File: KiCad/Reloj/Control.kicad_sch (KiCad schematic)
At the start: 67 parts, among them J13 Conn_01x08_SocketMPU, J14 Conn_01x04_Socket, J15 Screw_Terminal_01x02, J16 Conn_01x02, J17 Conn_01x06_Socket, J18 Conn_01x02, J19 Conn_01x03, J20 Conn_01x02, J21 Conn_01x02, Q1 BC548, Q2 BC548, Q3 BC548, Q4 BC548, Q5 BC548, Q6 BC548, Q7 BC548, SW1 SW_SPDT, SW2 SW_Push, SW3 SW_Push, SW4 SW_Push, SW5 SW_Push, U1 74HC14, U3 74HCT595

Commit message: Actualizo circuito y defino alimentaciones
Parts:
- added J1: Jack-DC, symbol Connector:Jack-DC
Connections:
- net 5v: now also U3.16 (VCC), J1.2
- net GND: now also J1.1
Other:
- note added: "ALIMENTACION EXTERNA Fte. 5Vdc"

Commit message: Agrego nueva numeracion de componentes e impresion de pdf
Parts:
- added C6: 0.1uF, symbol Device:C
- C5: value C -> 0.1uF
- R23: renamed from R18; value R_Small_US -> 330
- renumbered C6 to C1, C7 to C2, C8 to C3, C9 to C4, D4 to D1, D5 to D2, D2 to D3, D3 to D4, R4 to R1, R22 to R10, R23 to R11, R24 to R12, R25 to R13, R26 to R14, R19 to R15, R20 to R16, R12 to R17, R13 to R18, R14 to R19, R5 to R2, R15 to R20, R16 to R21, R17 to R22, R6 to R3, R7 to R4, R8 to R5, R9 to R6, R10 to R7, R11 to R8, R21 to R9
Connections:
- net 5v: now also C6.1
- net GND: now also C6.2
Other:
- note added: "R17 a R23 330 ohm"
- company: (none) -> Prof. Damián Rimoldi
- title: (none) -> Circuito Reloj

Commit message: Modifico circuito implementando CD4050
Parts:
- added C7: 0.1uF, symbol Device:C
- added C8: 0.1uF, Capacitor_SMD:C_0805_2012Metric, symbol Device:C
- added C9: 100uF 16V, Capacitor_SMD:CP_Elec_5x3.9, symbol Device:C_Polarized
- added U2: 4050, symbol 4xxx:4050
- U3: value 74HCT595 -> 74HC595
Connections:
- net 5v: now also C7.1, C8.1, C9.1, U2.1 (VCC)
- net GND: now also C7.2, C8.2, C9.2, U2.8 (VSS)
- net GPIO18: now also U2.5; no longer U3.11 (SRCLK)
- net GPIO23: now also U2.3; no longer U3.14 (SER)
- net GPIO5: now also U2.7; no longer U3.12 (RCLK)
- new net RCLK: U2.6, U3.12 (RCLK)
- new net SER: U2.2, U3.14 (SER)
- new net SRCLK: U2.4, U3.11 (SRCLK)
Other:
- note added: "BUFFER CD4050"
- moved on the sheet: J1

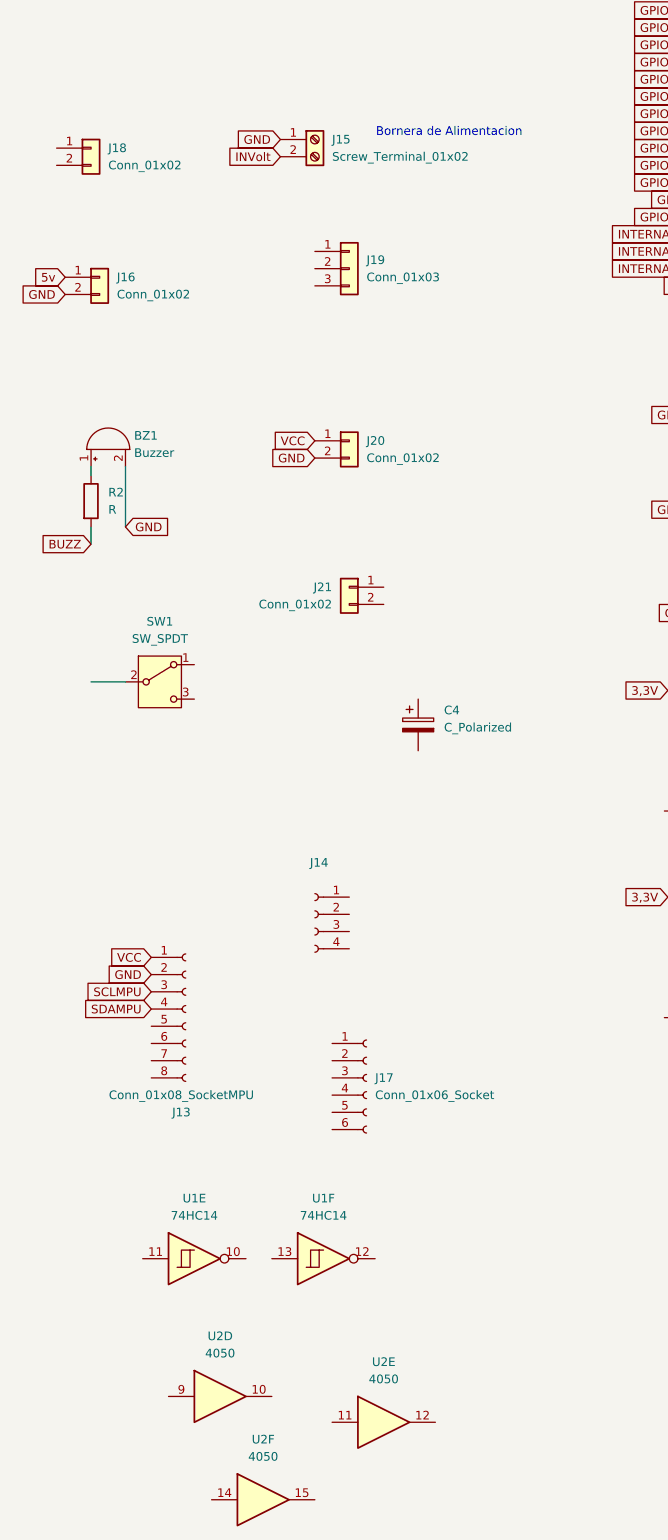
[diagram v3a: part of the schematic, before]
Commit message: Selecciono footprints y disposicion prelimar de PCB
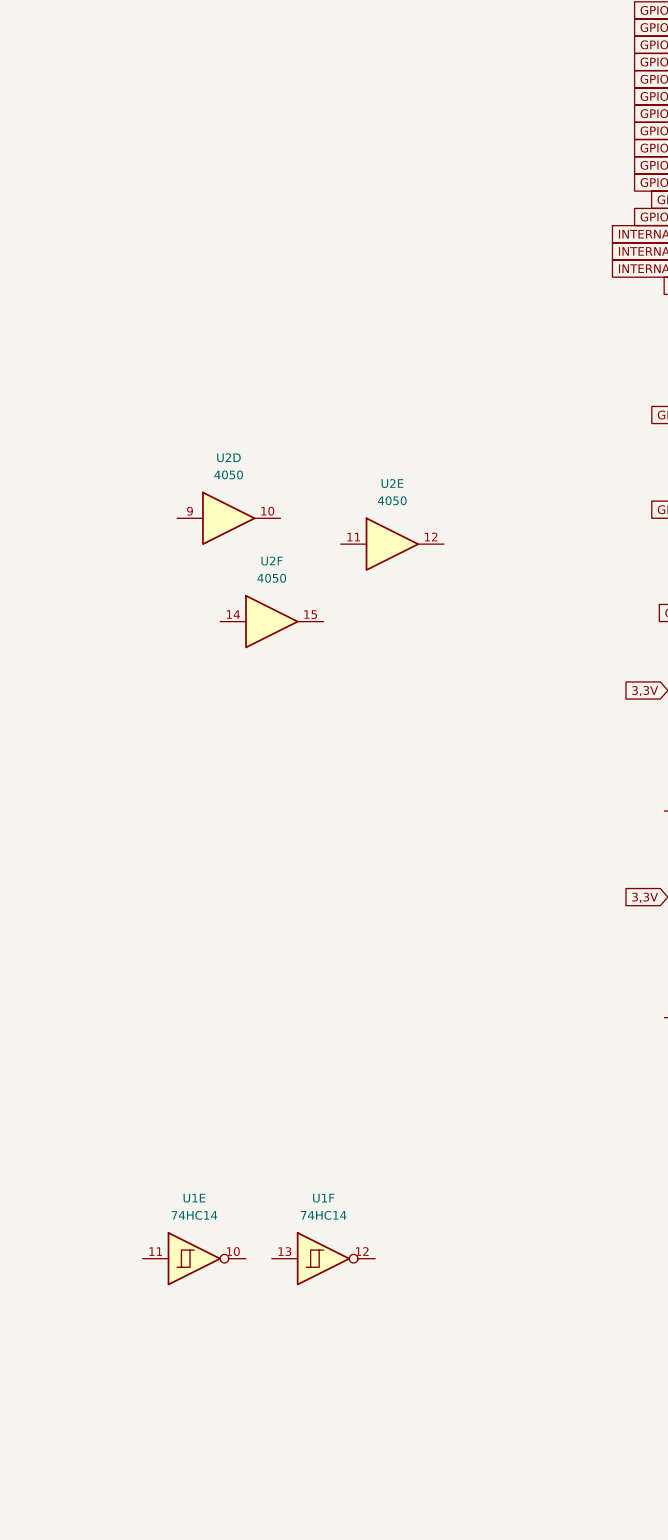
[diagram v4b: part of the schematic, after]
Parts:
- removed BZ1: Buzzer, Buzzer_Beeper:Buzzer_TDK_PS1240P02BT_D12.2mm_H6.5mm, symbol Device:Buzzer
- removed C4: C_Polarized, symbol Device:C_Polarized
- removed J13: Conn_01x08_SocketMPU, Connector_PinSocket_2.54mm:PinSocket_1x08_P2.54mm_Vertical, symbol Connector:Conn_01x08_Socket
- removed J14: Conn_01x04_Socket, Connector_PinSocket_2.54mm:PinSocket_1x04_P2.54mm_Vertical, symbol Connector:Conn_01x04_Socket
- removed J15: Screw_Terminal_01x02, TerminalBlock:TerminalBlock_bornier-2_P5.08mm, symbol Connector:Screw_Terminal_01x02
- removed J16, J20, J21: Conn_01x02, Connector_PinSocket_2.54mm:PinSocket_1x02_P2.54mm_Vertical, symbol Connector_Generic:Conn_01x02
- removed J17: Conn_01x06_Socket, Connector_PinSocket_2.54mm:PinSocket_1x06_P2.54mm_Vertical, symbol Connector:Conn_01x06_Socket
- removed J18: Conn_01x02, Connector_PinHeader_2.54mm:PinHeader_1x02_P2.54mm_Vertical, symbol Connector_Generic:Conn_01x02
- removed J19: Conn_01x03, Connector_PinSocket_2.54mm:PinSocket_1x03_P2.54mm_Vertical, symbol Connector_Generic:Conn_01x03
- removed R2: R, Resistor_SMD:R_0805_2012Metric_Pad1.20x1.40mm_HandSolder, symbol Device:R
- removed SW1: SW_SPDT, Button_Switch_THT:SW_Slide_SPDT_Straight_CK_OS102011MS2Q, symbol Switch:SW_SPDT
- C1, C2, C3, C4, C5, C6, C7: footprint (none) -> Capacitor_THT:C_Disc_D5.0mm_W2.5mm_P2.50mm
- C8: footprint Capacitor_SMD:C_0805_2012Metric -> Capacitor_THT:C_Disc_D5.0mm_W2.5mm_P2.50mm
- C9: footprint Capacitor_SMD:CP_Elec_5x3.9 -> Capacitor_THT:CP_Radial_D6.3mm_P2.50mm
- D1, D2, D3, D4: footprint (none) -> LED_THT:LED_D3.0mm
- J1: footprint (none) -> Connector_BarrelJack:BarrelJack_Horizontal
- R1, R10, R11, R12, R13, R14, R15, R16, R2, R23, R27, R3, R4, R5, R6, R7, R8, R9: footprint (none) -> Resistor_THT:R_Axial_DIN0204_L3.6mm_D1.6mm_P5.08mm_Horizontal
- R17, R18, R19, R20, R21, R22: value R_Small_US -> 330; footprint (none) -> Resistor_THT:R_Axial_DIN0204_L3.6mm_D1.6mm_P5.08mm_Horizontal
- SW2, SW3, SW4, SW5: footprint (none) -> Button_Switch_THT:SW_PUSH_6mm_H4.3mm
- U1: footprint (none) -> Package_DIP:DIP-14_W7.62mm_Socket_LongPads
- U2, U3: footprint (none) -> Package_DIP:DIP-16_W7.62mm_Socket_LongPads
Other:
- note removed: "Bornera de Alimentacion"
- moved on the sheet: U2D, U2E, U2F

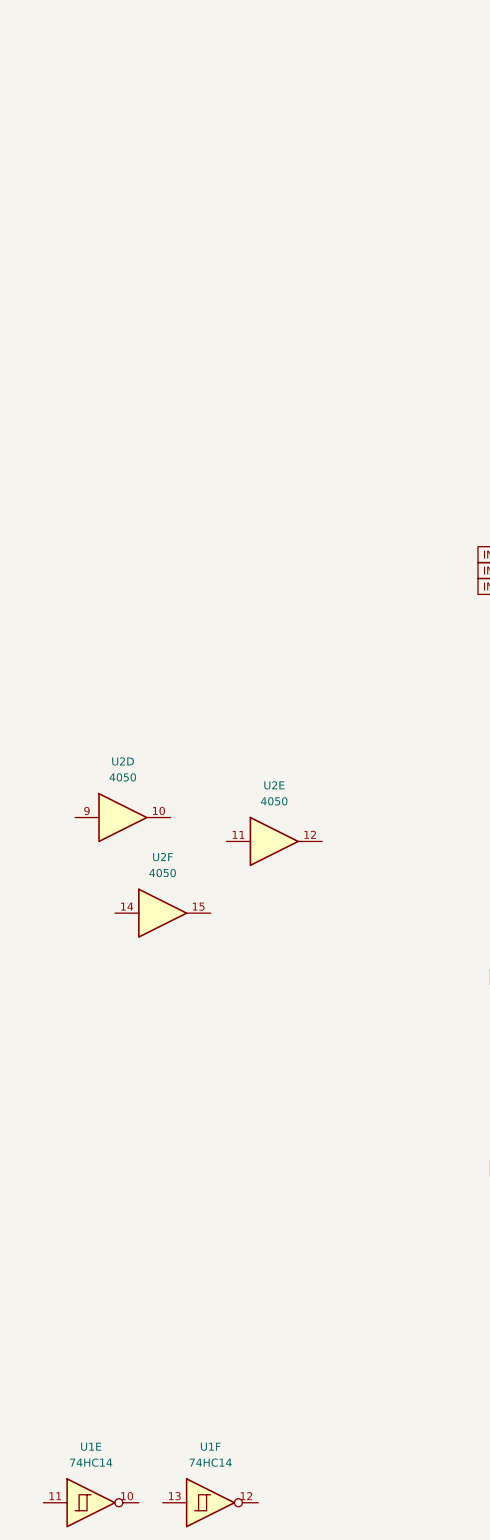
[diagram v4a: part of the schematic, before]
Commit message: Agrego version 3 placas, distribucion principal y conectores
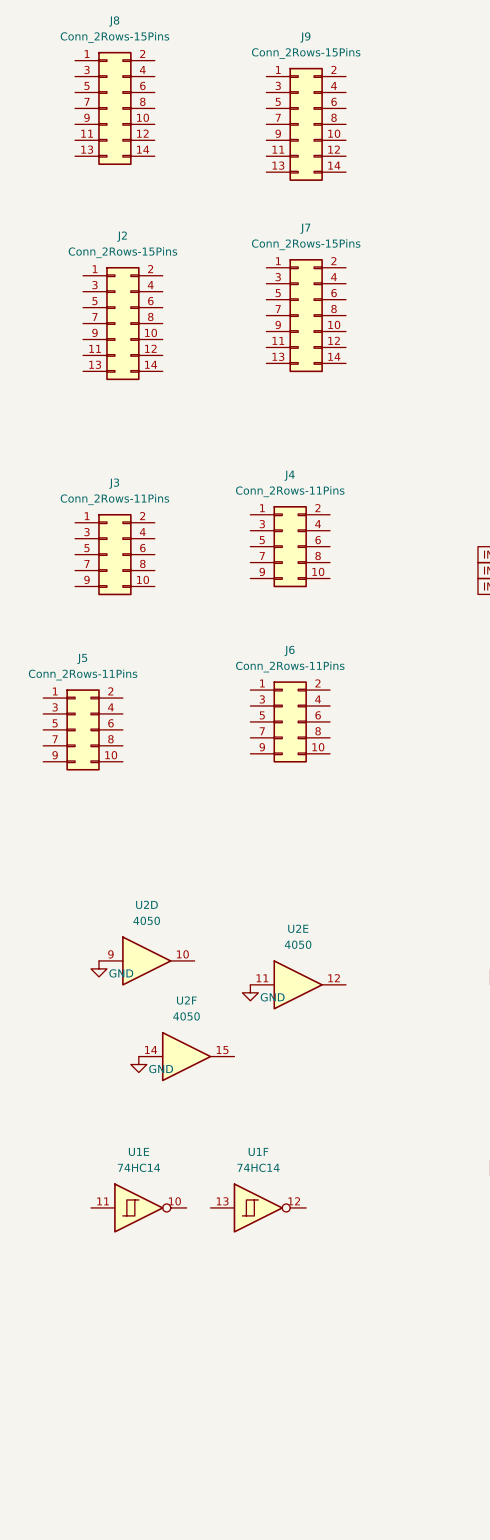
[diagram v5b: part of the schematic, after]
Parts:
- added J2, J7, J8, J9: Conn_2Rows-15Pins, Connector_IDC:IDC-Header_2x07_P2.54mm_Vertical, symbol Connector_Generic:Conn_2Rows-15Pins
- added J3, J4, J5, J6: Conn_2Rows-11Pins, Connector_IDC:IDC-Header_2x05_P2.54mm_Vertical, symbol Connector_Generic:Conn_2Rows-11Pins
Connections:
- net GND: now also U2.11, U2.14, U2.9
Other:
- moved on the sheet: U1E, U1F, U2D, U2E, U2F
